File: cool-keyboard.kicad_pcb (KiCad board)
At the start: 2 copper layers, 81.8 x 81 mm, 22 parts, among them SW1 SW_Push_45deg, SW10 SW_Push_45deg, SW13 RotaryEncoder_Switch, SW2 SW_Push_45deg, SW3 SW_Push_45deg, SW4 SW_Push_45deg, SW5 SW_Push_45deg, SW6 SW_Push_45deg, SW7 SW_Push_45deg, SW8 SW_Push_45deg, SW9 SW_Push_45deg, U2 MOUDLE-SEEEDUINO-XIAO

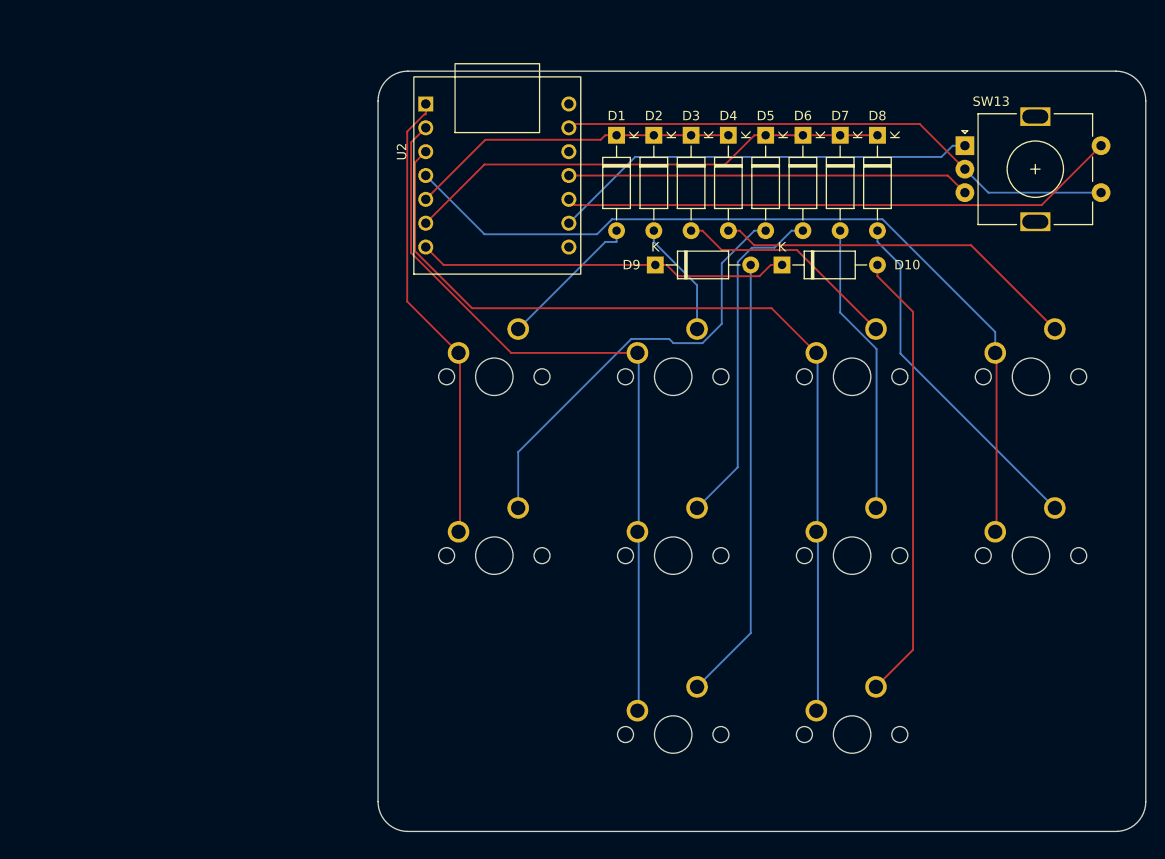
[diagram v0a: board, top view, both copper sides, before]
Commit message: fix mcu placement
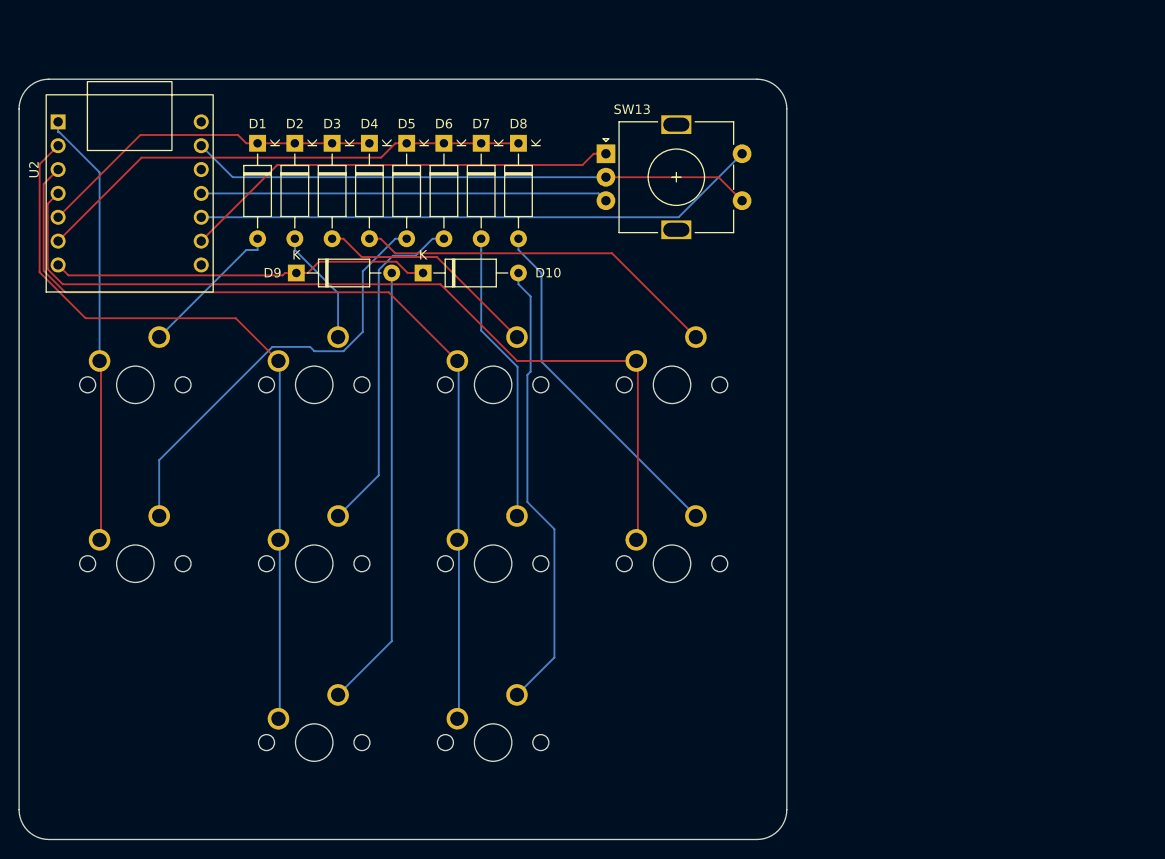
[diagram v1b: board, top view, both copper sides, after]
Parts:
- moved U2 39.2 mm to (117.2, 69.4)
- moved D1 38.2 mm to (130.8, 64.0)
- moved D10 38.2 mm to (148.5, 77.9)
- moved D2 38.2 mm to (134.8, 64.0)
- moved D3 38.2 mm to (138.8, 64.0)
- moved D4 38.2 mm to (142.7, 64.0)
- moved D5 38.2 mm to (146.7, 64.0)
- moved D6 38.2 mm to (150.7, 64.0)
- moved D7 38.2 mm to (154.7, 64.0)
- moved D8 38.2 mm to (158.6, 64.0)
- moved D9 38.2 mm to (135.0, 77.9)
- moved SW1 38.2 mm to (117.8, 89.8)
- moved SW10 38.2 mm to (155.9, 127.9)
- moved SW13 38.2 mm to (167.9, 65.2)
- moved SW2 38.2 mm to (136.9, 89.8)
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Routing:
- net COL3: track 90.3 -> 94.4 mm
- net COL0: track 48.9 -> 46.5 mm
- net ROW0: track 35.1 -> 37.1 mm
- net EC11A: track 45.6 -> 46.9 mm
- net ROW1: track 52.0 -> 53.3 mm
- net COL1: track 80.8 -> 82.0 mm
- net COL2: track 96.6 -> 97.8 mm
- net EC11SW: track 59.5 -> 60.4 mm
- net ROW2: track 39.7 -> 40.4 mm

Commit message: add ssd1306
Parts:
- removed SW13: RotaryEncoder_Switch, Rotary_Encoder:RotaryEncoder_Alps_EC11E-Switch_Vertical_H20mm
- added Brd1: SSD1306, SSD1306:128x64OLED, F.Cu at (140.5, 63.5)
- moved D10 25.8 mm to (174.0, 73.8)
- moved D2 25.8 mm to (160.3, 60.0)
- moved D4 25.8 mm to (168.3, 60.0)
- moved D6 25.8 mm to (176.2, 60.0)
- moved D8 25.8 mm to (184.2, 60.0)
- moved D1 25.8 mm to (156.4, 60.0)
- moved D3 25.8 mm to (164.3, 60.0)
- moved D5 25.8 mm to (172.2, 60.0)
- moved D7 25.8 mm to (180.2, 60.0)
- moved D9 25.8 mm to (160.5, 73.8)
- moved U2 6.58 mm to (117.6, 62.8)
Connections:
- U2 pad 10: EC11SW -> ROW2
- U2 pad 11: EC11B -> unconnected-(U2-PA6_A10_D10_MOSI-Pad11)
- U2 pad 12: unconnected-(U2-3V3-Pad12) -> SCR3V3
- U2 pad 5: ROW0 -> Net-(Brd1-SDA)
- U2 pad 6: ROW1 -> Net-(Brd1-SCL)
- U2 pad 7: ROW2 -> unconnected-(U2-PB08_A6_D6_TX-Pad7)
- U2 pad 8: unconnected-(U2-PB09_A7_D7_RX-Pad8) -> ROW0
- U2 pad 9: EC11A -> ROW1
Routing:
- net EC11SW: track 60.4 -> 0.00 mm
- net EC11A: track 46.9 -> 0.00 mm
- net GND: track 60.0 -> 13.6 mm
- net EC11B: track 43.4 -> 0.00 mm
- net Net-(Brd1-SDA): track 0.00 -> 40.9 mm
- net Net-(Brd1-SCL): track 0.00 -> 38.4 mm
- net Net-(D5-A): track 46.2 -> 73.6 mm
- net Net-(D1-A): track 15.5 -> 42.0 mm
- net Net-(D6-A): track 36.3 -> 59.1 mm
- net Net-(D9-A): track 47.3 -> 67.2 mm
- net Net-(D4-A): track 39.1 -> 20.9 mm
- net SCR3V3: track 0.00 -> 17.4 mm
- net ROW2: track 40.4 -> 57.2 mm
- net Net-(D2-A): track 12.4 -> 26.9 mm
- net Net-(D7-A): track 31.2 -> 42.6 mm
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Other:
- board size 81.8 x 81 mm -> 81.9 x 87.4 mm

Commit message: 3d screen + design fix
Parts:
- moved Brd1 31.8 mm to (172.3, 64.3)
- moved D1 27.8 mm to (128.8, 63.4)
- moved D10 27.8 mm to (146.4, 77.2)
- moved D2 27.8 mm to (132.7, 63.4)
- moved D3 27.8 mm to (136.7, 63.4)
- moved D4 27.8 mm to (140.7, 63.4)
- moved D5 27.8 mm to (144.7, 63.4)
- moved D6 27.8 mm to (148.6, 63.4)
- moved D7 27.8 mm to (152.6, 63.4)
- moved D8 27.8 mm to (156.6, 63.4)
- moved D9 27.8 mm to (132.9, 77.2)
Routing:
- net Net-(Brd1-SDA): track 40.9 -> 72.4 mm
- net GND: track 13.6 -> 45.1 mm
- net Net-(Brd1-SCL): track 38.4 -> 69.9 mm
- net SCR3V3: track 17.4 -> 48.9 mm
- net ROW1: track 63.2 -> 33.2 mm
- net ROW2: track 57.2 -> 29.5 mm
- net Net-(D5-A): track 73.6 -> 46.0 mm
- net Net-(D1-A): track 42.0 -> 14.6 mm
- net ROW0: track 47.4 -> 22.4 mm
- net Net-(D6-A): track 59.1 -> 36.1 mm
- net Net-(D4-A): track 20.9 -> 41.4 mm
- net Net-(D9-A): track 67.2 -> 47.4 mm
- net Net-(D2-A): track 26.9 -> 13.9 mm
- net Net-(D3-A): track 16.9 -> 29.1 mm
- net Net-(D10-A): track 59.6 -> 48.3 mm
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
